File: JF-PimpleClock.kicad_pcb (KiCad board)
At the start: 2 copper layers, 190.4 x 298.6 mm, 56 parts, among them J1 Conn_01x06_Female, J2 Conn_01x02, J3 Conn_01x02, J4 USB_B_Micro, Q1 Q_PMOS_DSG, SW1 SW_Push, SW2 SW_Push, SW3 SW_Push, SW4 SW_Push, U1 ATmega328-P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

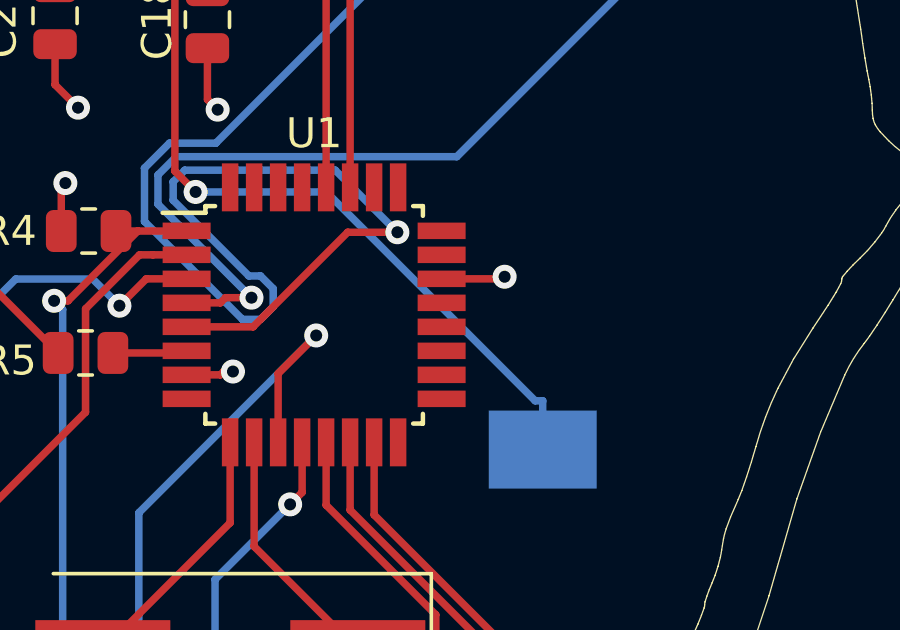
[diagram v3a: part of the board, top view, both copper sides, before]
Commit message: small circuit tweak for fixing missing vcc/avcc ref for bootloader
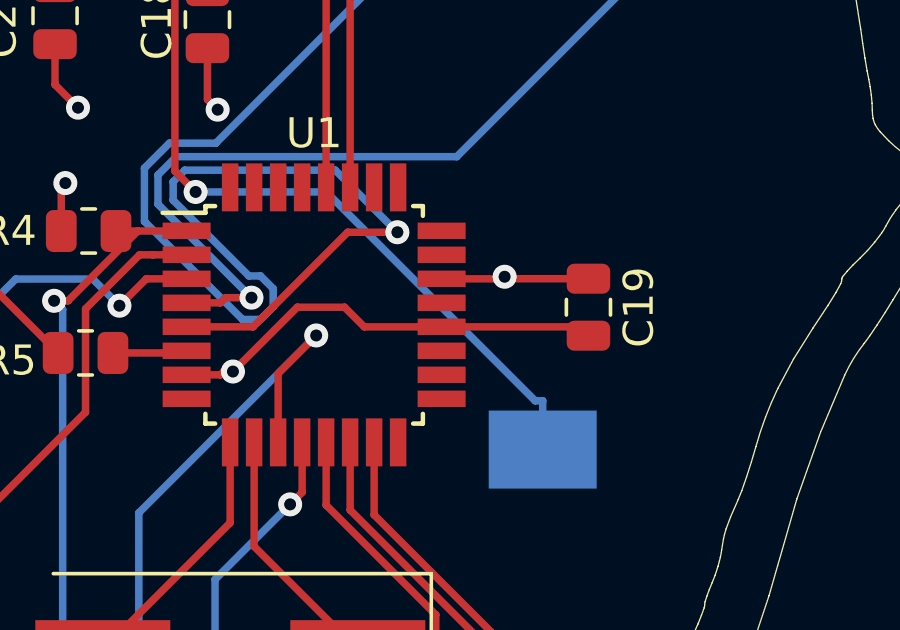
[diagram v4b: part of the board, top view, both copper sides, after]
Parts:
- added C19: 100nF, Capacitor_SMD:C_0805_2012Metric, F.Cu at (165.9, -114.6)
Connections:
- U1 pad 20: unconnected-(U1-Pad20) -> /5v
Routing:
- net /5v: track 248.6 -> 261.8 mm
- net GND: track 18.4 -> 21.2 mm

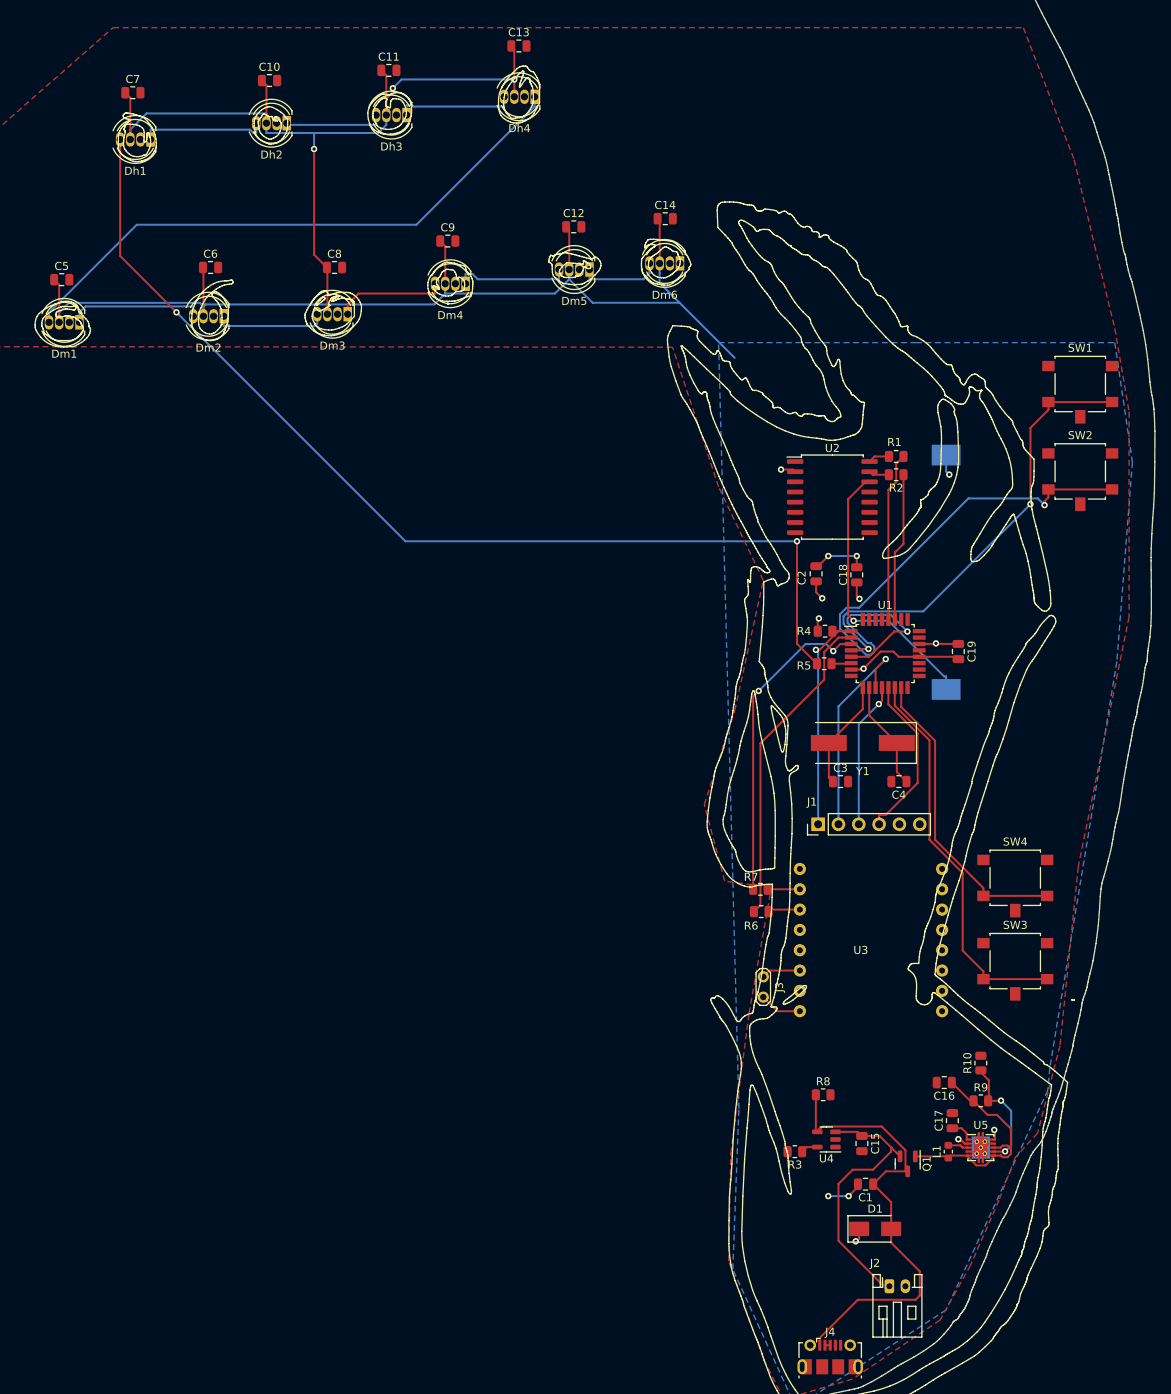
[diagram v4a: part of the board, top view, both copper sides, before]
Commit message: revision 2, changed some parts for making it easier to manufacture, fixed the issue with the wrong atmega footprint, added more test points
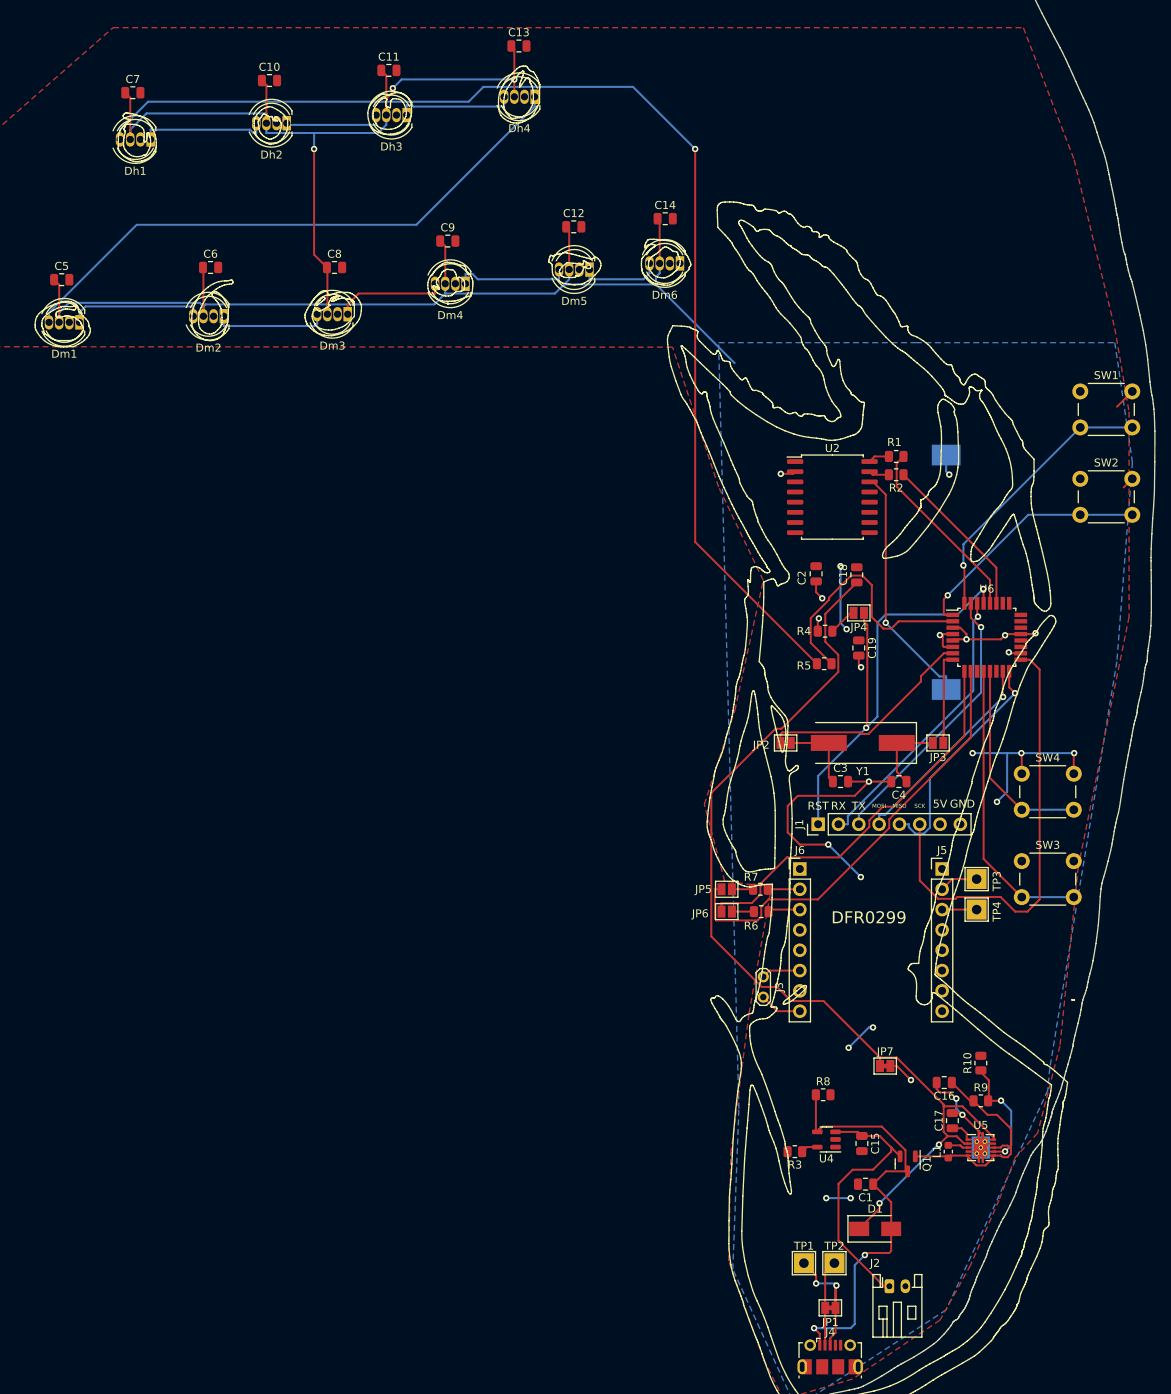
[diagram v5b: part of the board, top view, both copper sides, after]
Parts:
- removed U1: ATmega328-P, Package_QFP:TQFP-32_7x7mm_P0.8mm
- removed U3: DFR0299, Arduino_Nano:DFPlayer_V2
- added J5: Conn_01x08_Female, Connector_PinHeader_2.54mm:PinHeader_1x08_P2.54mm_Vertical, F.Cu at (163.8, -87.4)
- added J6: Conn_01x08_Female, Connector_PinHeader_2.54mm:PinHeader_1x08_P2.54mm_Vertical, F.Cu at (146.1, -87.4)
- added JP1: Data_Bridge, Jumper:SolderJumper-2_P1.3mm_Bridged_Pad1.0x1.5mm, F.Cu at (149.9, -32.5)
- added JP2: XTAL_1, Jumper:SolderJumper-2_P1.3mm_Open_Pad1.0x1.5mm, F.Cu at (144.3, -103.1)
- added JP3: XTAL_2, Jumper:SolderJumper-2_P1.3mm_Open_Pad1.0x1.5mm, F.Cu at (163.3, -103.1)
- added JP4: Reset_RSTR, Jumper:SolderJumper-2_P1.3mm_Open_Pad1.0x1.5mm, F.Cu at (153.4, -119.4)
- added JP5: DFR_RX, Jumper:SolderJumper-2_P1.3mm_Open_Pad1.0x1.5mm, F.Cu at (136.9, -84.8)
- added JP6: DFR_TX, Jumper:SolderJumper-2_P1.3mm_Open_Pad1.0x1.5mm, F.Cu at (136.9, -82.0)
- added JP7: Power_Output, Jumper:SolderJumper-2_P1.3mm_Bridged_Pad1.0x1.5mm, F.Cu at (156.7, -62.7)
- added TP1: D+, TestPoint:TestPoint_THTPad_2.5x2.5mm_Drill1.2mm, F.Cu at (146.6, -38.1)
- added TP2: D-, TestPoint:TestPoint_THTPad_2.5x2.5mm_Drill1.2mm, F.Cu at (150.4, -38.1)
- added TP3: USB-, TestPoint:TestPoint_THTPad_2.5x2.5mm_Drill1.2mm, F.Cu at (168.1, -86.1)
- added TP4: USB+, TestPoint:TestPoint_THTPad_2.5x2.5mm_Drill1.2mm, F.Cu at (168.1, -82.3)
- added U6: ATmega328P-A, Package_QFP:TQFP-32_7x7mm_P0.8mm, F.Cu at (169.4, -116.3)
- J1: value Conn_01x06_Female -> Conn_01x08_Female; footprint Connector_PinHeader_2.54mm:PinHeader_1x06_P2.54mm_Vertical -> Connector_PinHeader_2.54mm:PinHeader_1x08_P2.54mm_Vertical
- SW1, SW2, SW3, SW4: footprint Button_Switch_SMD:SW_SPST_B3S-1100 -> Button_Switch_THT:SW_PUSH_6mm_H5mm
- moved SW4 14.0 mm to (173.8, -99.3)
- moved SW3 13.5 mm to (173.8, -88.4)
- moved C19 12.5 mm to (153.4, -115.0)
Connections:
- C18 pad 1: /5v -> Net-(C18-Pad1)
- D1 pad 1: /5v -> Net-(C18-Pad1)
- J1 pad 2: /MOSI -> /MCU_RX
- J1 pad 3: /MISO -> /MCU_TX
- J1 pad 4: /SCK -> /MOSI
- J1 pad 5: /5v -> /MISO
- J1 pad 6: GND -> /SCK
- J4 pad 3: Net-(J4-Pad2) -> Net-(J4-Pad3)
- R4 pad 1: /RESET -> Net-(R4-Pad1)
- R6 pad 2: /MCU_RX -> Net-(R6-Pad2)
- R7 pad 2: /MCU_TX -> Net-(R7-Pad2)
- U5 pad 10: /5v -> Net-(C18-Pad1)
- U5 pad 2: /5v -> Net-(C18-Pad1)
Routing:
- net Net-(C18-Pad1): track 0.00 -> 124.3 mm, vias 0 -> 2
- net GND: track 21.2 -> 105.6 mm, vias 6 -> 19
- net /MCU_SSTX: track 0.00 -> 55.7 mm
- net /MCU_SSRX: track 0.00 -> 49.4 mm
- net /SW2: track 72.2 -> 31.0 mm, vias 2 -> 1
- net /SCK: track 21.1 -> 56.1 mm
- net /RESET: track 28.0 -> 59.7 mm, vias 1 -> 2
- net /NeoPixel_D: track 2.49 -> 32.4 mm
- net Net-(U6-Pad7): track 0.00 -> 27.4 mm
- net /SW1: track 58.4 -> 34.6 mm, vias 2 -> 1
- net Net-(Dh1-Pad4): track 130.3 -> 149.2 mm, vias 2 -> 1
- net Net-(J4-Pad3): track 0.00 -> 16.3 mm, vias 0 -> 2
- net /5v: track 261.8 -> 248.2 mm, vias 11 -> 10
- net /SW4: track 38.3 -> 25.4 mm
- net /SW3: track 49.0 -> 36.7 mm
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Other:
- board text added: "5V"
- board text added: "DFR0299"
- board text added: "GND"
- board text added: "MISO"
- board text added: "MOSI"
- board text added: "RST"
- board text added: "RX"
- board text added: "SCK"
- board text added: "TX"
